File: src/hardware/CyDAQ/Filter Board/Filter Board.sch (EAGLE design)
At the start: 218 parts, among them J1 DCJ0202, J10 Vout_HEADER, J11 5V0_SENSOR, J12 3V3_SENSOR, J13 1V8_SENSOR, J14 BRKOUT_JD, J15 BRKOUT_JC, J16 BRKOUT_JB, J17 BRKOUT_JF, J18 5V0_CONN, J19 3V3_CONN, J2 ZYBO_JF, J20 1V8_CONN, J3 ZYBO_JE, J4 ZYBO_JD, J5 ZYBO_JC, J6 ZYBO_JB, J7 A_XADC, J8 SJ1-3523N, J9 Vin_HEADER, U1 TPS54531DDARDDA8_3P1X2P4-L, U10 CD74HCT4051, U11 CD74HCT4051, U12 OPA4197, U13 OPA4197, U14 OPA4197, U15 OPA4197, U16 OPA4197, U17 CD74HCT4053, U18 CD74HCT4051, U19 OPA2197, U2 VS-50WQ04FNPBFDPAK-L, U3 TPS56339, U4 TPS56339, U5 LM43601PWPR, U6 X9258_A, U7 X925_B, U8 X9258_C, U9 X9258_D

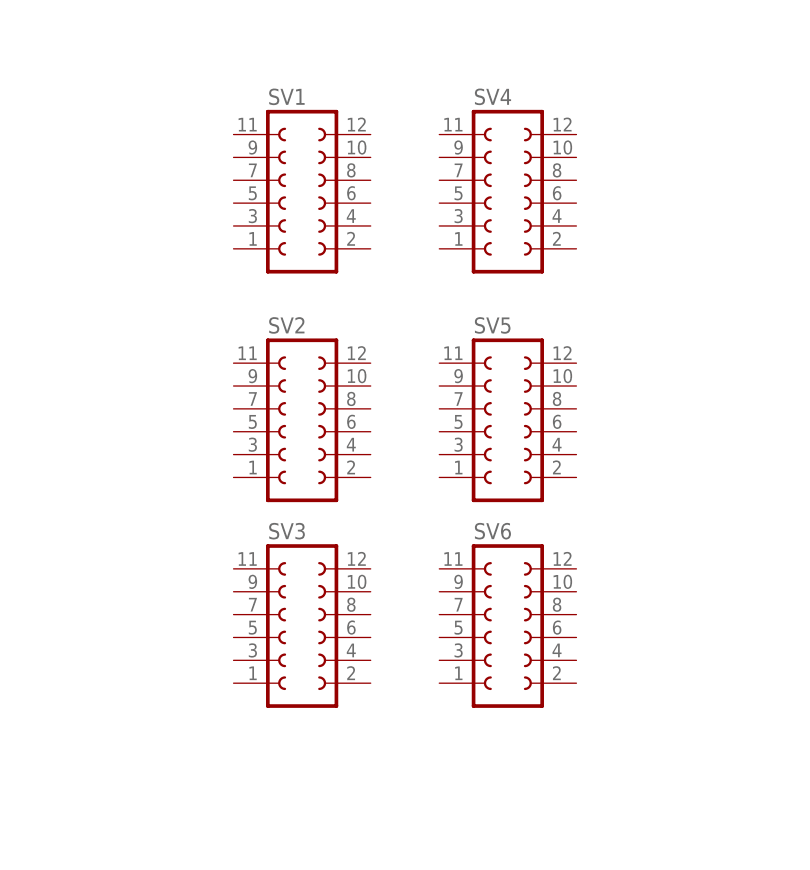
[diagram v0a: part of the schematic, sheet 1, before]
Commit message: Placed components and started routing
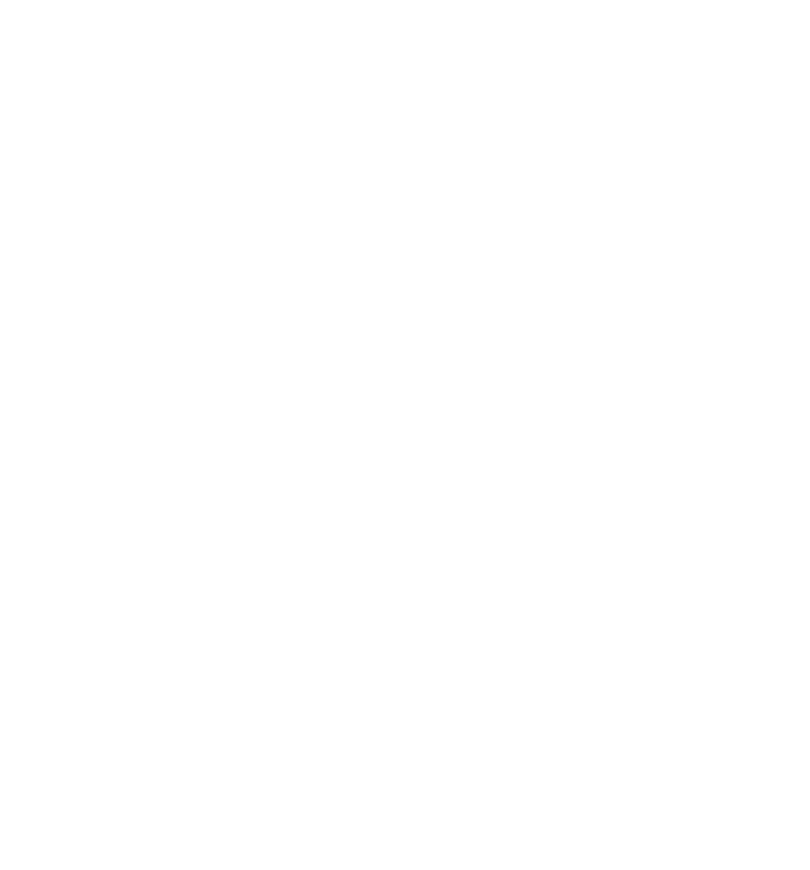
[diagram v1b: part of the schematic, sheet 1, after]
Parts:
- removed SV1, SV2, SV3, SV4, SV5, SV6: (no value), con-lsta:FE06-2
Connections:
- removed net N$60: C44.2, J7.3, J7.4, R61.2, U12_C.OUT, U9_VR1.H, U9_VR1.W
- net 1V8SENSOR_IN: now also U18.A0; no longer U18.A2
- net 3V3SENSOR_IN: now also U18.A1; no longer U18.A0
- net 5V0SENSOR_IN: now also U18.A2; no longer U18.A1
- net GND: now also C44.2, J7.3, J7.4, R61.2, U12_C.OUT, U9_VR1.H, U9_VR1.W
- net SCL: now also R14.1; no longer R15.1
- net SDA: now also R15.1; no longer R14.1
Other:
- note added: "I2C Pullups"
- moved on the sheet: R16, R29

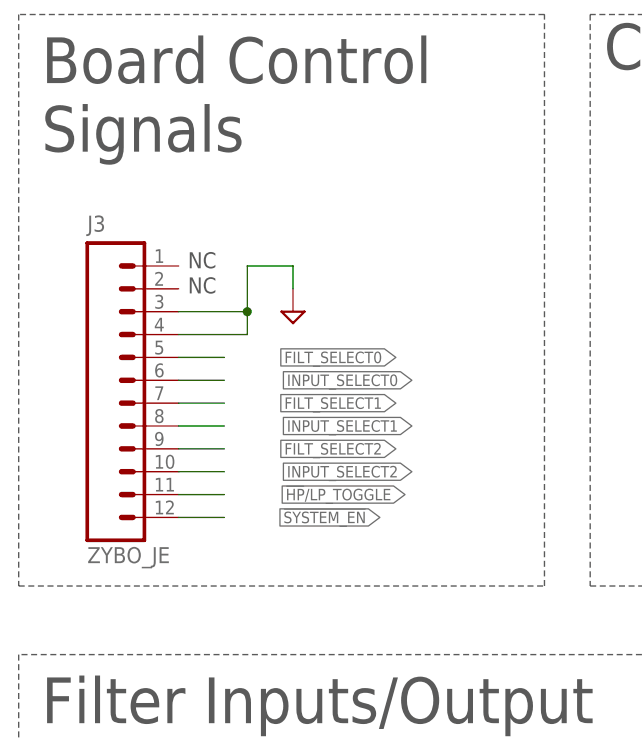
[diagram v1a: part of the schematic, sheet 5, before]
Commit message: Finished routing BP filter
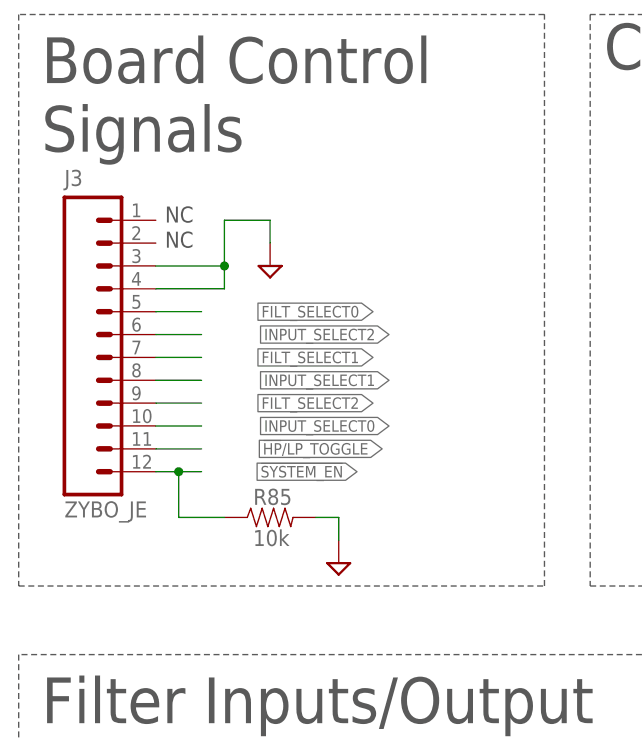
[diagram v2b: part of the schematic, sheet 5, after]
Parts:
- added R85: 10k, Resistors:SMD_0805
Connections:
- new net BP6_HPOUT: C44.2, R61.2, U12_B.OUT, U9_VR1.H, U9_VR1.W
- net !SYSTEM_EN: now also R85.1
- net BP6_OUT: now also U13_D.-IN, U13_D.OUT; no longer U14_A.-IN, U14_A.OUT
- net GND: now also R85.2, U12_B.+IN, U13_C.+IN, U14_B.+IN; no longer C44.2, R61.2, U12_C.OUT, U12_D.+IN, U13_D.+IN, U14_D.+IN, U9_VR1.H, U9_VR1.W
- net HP2_OUT1: now also U14_A.OUT; no longer U14_B.OUT
- net INPUT_SELECT0: now also J3.10; no longer J3.6
- net INPUT_SELECT2: now also J3.6; no longer J3.10
- net LP2_OUT1: now also U14_C.OUT; no longer U14_D.OUT
- net N$22: now also U14_D.+IN; no longer U12_A.+IN
- net N$23: now also U14_D.-IN, U14_D.OUT; no longer U12_A.-IN, U12_A.OUT
- net N$24: now also U12_A.-IN; no longer U12_B.-IN
- net N$25: now also U14_A.+IN; no longer U14_B.+IN
- net N$26: now also U14_A.-IN; no longer U14_B.-IN
- net N$28: now also U14_B.-IN; no longer U14_C.-IN
- net N$29: now also U14_B.OUT; no longer U14_C.OUT
- net N$30: now also U14_C.-IN; no longer U14_D.-IN
- net N$57: now also U12_A.+IN; no longer U12_B.+IN
- net N$58: now also U12_A.OUT, U9_VR2.H, U9_VR2.W; no longer U12_B.OUT, U9_VR0.H, U9_VR0.W
- net N$59: now also U12_B.-IN, U9_VR2.L; no longer U12_C.-IN, U9_VR0.L
- net N$61: now also U12_C.-IN; no longer U12_D.-IN
- net N$62: now also U12_C.OUT, U9_VR0.H, U9_VR0.W; no longer U12_D.OUT, U9_VR2.H, U9_VR2.W
- net N$63: now also U12_D.+IN, U9_VR0.L; no longer U13_A.+IN, U9_VR2.L
- net N$64: now also U12_D.-IN, U12_D.OUT; no longer U13_A.-IN, U13_A.OUT
- net N$65: now also U13_A.-IN; no longer U13_C.-IN
- net N$66: now also U13_A.+IN; no longer U13_C.+IN
- net N$67: now also U13_A.OUT; no longer U13_C.OUT
- net N$68: now also U13_C.-IN; no longer U13_B.-IN
- net N$69: now also U13_C.OUT; no longer U13_B.OUT
- net N$70: now also U13_B.-IN; no longer U13_D.-IN
- net N$71: now also U13_B.OUT; no longer U13_D.OUT
- net N$72: now also U13_D.+IN; no longer U14_A.+IN
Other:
- moved on the sheet: J3, U12_B, U12_C, U12_D, U13_A, U13_B, U13_C, U13_D, U14_B, U14_C, U14_D, U9_VR0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

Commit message: Continued routing ~ 80% done
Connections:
- net FILTER_IN: now also U16_B.+IN; no longer U16_C.+IN
- net FILTER_OUT_BUFF: now also U16_C.-IN, U16_C.OUT; no longer U16_D.-IN, U16_D.OUT
- net GND: now also U15_D.+IN, U16_D.+IN, U6_VR1.L, U7_VR3.L; no longer U15_B.+IN, U16_B.+IN, U6_VR2.L, U7_VR1.L
- net HP2_OUT2: now also U15_B.OUT, U8_VR3.H, U8_VR3.W; no longer U15_A.OUT, U8_VR2.H, U8_VR2.W
- net HP2_OUT3: now also U15_A.OUT; no longer U15_D.OUT
- net LP1_IN: now also U6_VR2.H, U6_VR2.W; no longer U6_VR1.H, U6_VR1.W
- net LP1_OUT: now also U6_VR2.L; no longer U6_VR1.L
- net LP2_OUT1: now also U14_B.OUT; no longer U14_C.OUT
- net LP2_OUT2: now also U15_D.OUT; no longer U15_C.OUT
- net LP2_OUT3: now also U16_D.OUT; no longer U16_B.OUT
- net N$22: now also U6_VR1.H, U6_VR1.W; no longer U6_VR2.H, U6_VR2.W
- net N$28: now also U14_C.-IN; no longer U14_B.-IN
- net N$29: now also U14_C.OUT, U7_VR1.H, U7_VR1.W; no longer U14_B.OUT, U7_VR3.H, U7_VR3.W
- net N$30: now also U14_B.-IN, U7_VR1.L; no longer U14_C.-IN, U7_VR3.L
- net N$31: now also U15_B.+IN; no longer U15_A.+IN
- net N$32: now also U15_B.-IN; no longer U15_A.-IN
- net N$34: now also U15_C.-IN, U8_VR3.L; no longer U15_B.-IN, U8_VR2.L
- net N$35: now also U15_C.OUT, U8_VR2.H, U8_VR2.W; no longer U15_B.OUT, U8_VR3.H, U8_VR3.W
- net N$36: now also U15_D.-IN, U8_VR2.L; no longer U15_C.-IN, U8_VR3.L
- net N$37: now also U15_A.+IN; no longer U15_D.+IN
- net N$38: now also U15_A.-IN; no longer U15_D.-IN
- net N$42: now also U16_D.-IN; no longer U16_B.-IN
- net N$43: now also U16_C.+IN; no longer U16_D.+IN
- net N$72: now also U7_VR3.H, U7_VR3.W; no longer U7_VR1.H, U7_VR1.W
- net VIN_BUFFERED: now also U16_B.-IN, U16_B.OUT; no longer U16_C.-IN, U16_C.OUT
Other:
- note removed: "TODO: Add voltage protection"
- moved on the sheet: U14_B, U14_C, U15_A, U15_B, U15_C, U15_D, U16_C, U6_VR1, U6_VR2, U8_VR2, U8_VR3

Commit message: Used Gateswap magic to clean up some routing
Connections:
- net HP2_OUT1: now also U7_VR1.H, U7_VR1.W; no longer U7_VR2.H, U7_VR2.W
- net LP2_OUT1: now also U14_C.OUT; no longer U14_B.OUT
- net N$28: now also U14_B.-IN, U7_VR1.L; no longer U14_C.-IN, U7_VR2.L
- net N$29: now also U14_B.OUT, U7_VR2.H, U7_VR2.W; no longer U14_C.OUT, U7_VR1.H, U7_VR1.W
- net N$30: now also U14_C.-IN, U7_VR2.L; no longer U14_B.-IN, U7_VR1.L
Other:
- moved on the sheet: U14_B, U14_C, U7_VR1, U7_VR2
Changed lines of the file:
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@@
 </instance>
 <instance part="SUPPLY58" gate="GND" x="172.72" y="22.86" smashed="yes"/>
-<instance part="U7" gate="_VR2" x="116.84" y="220.98" smashed="yes" rot="R90">
+<instance part="U7" gate="_VR1" x="116.84" y="220.98" smashed="yes" rot="R90">
 <attribute name="NAME" x="106.934" y="225.552" size="1.778" layer="95"/>
 <attribute name="VALUE" x="113.03" y="215.646" size="1.778" layer="95"/>
@@
 <attribute name="NAME" x="92.71" y="207.518" size="1.778" layer="95"/>
 </instance>
-<instance part="U14" gate="_C" x="137.16" y="205.74" smashed="yes">
+<instance part="U14" gate="_B" x="137.16" y="205.74" smashed="yes">
 <attribute name="VALUE" x="140.97" y="202.438" size="1.778" layer="96"/>
 <attribute name="NAME" x="140.97" y="207.518" size="1.778" layer="95"/>
 </instance>
-<instance part="U14" gate="_B" x="187.96" y="205.74" smashed="yes">
+<instance part="U14" gate="_C" x="187.96" y="205.74" smashed="yes">
 <attribute name="VALUE" x="191.77" y="202.438" size="1.778" layer="96"/>
 <attribute name="NAME" x="191.77" y="207.518" size="1.778" layer="95"/>
@@
 <attribute name="NAME" x="191.77" y="103.378" size="1.778" layer="95"/>
 </instance>
-<instance part="U7" gate="_VR1" x="167.64" y="220.98" smashed="yes" rot="R90">
+<instance part="U7" gate="_VR2" x="167.64" y="220.98" smashed="yes" rot="R90">
 <attribute name="NAME" x="157.988" y="225.298" size="1.778" layer="95"/>
 <attribute name="VALUE" x="164.084" y="215.9" size="1.778" layer="95"/>
@@
 <wire x1="127" y1="200.66" x2="127" y2="203.2" width="0.1524" layer="91"/>
 <wire x1="127" y1="203.2" x2="129.54" y2="203.2" width="0.1524" layer="91"/>
-<pinref part="U14" gate="_C" pin="+IN"/>
+<pinref part="U14" gate="_B" pin="+IN"/>
 </segment>
 <segment>
@@
 <wire x1="177.8" y1="200.66" x2="177.8" y2="203.2" width="0.1524" layer="91"/>
 <wire x1="177.8" y1="203.2" x2="180.34" y2="203.2" width="0.1524" layer="91"/>
-<pinref part="U14" gate="_B" pin="+IN"/>
+<pinref part="U14" gate="_C" pin="+IN"/>
 </segment>
 <segment>
@@
 <net name="HP2_OUT1" class="0">
 <segment>
-<pinref part="U7" gate="_VR2" pin="W"/>
+<pinref part="U7" gate="_VR1" pin="W"/>
 <wire x1="116.84" y1="226.06" x2="116.84" y2="228.6" width="0.1524" layer="91"/>
 <wire x1="116.84" y1="228.6" x2="104.14" y2="228.6" width="0.1524" layer="91"/>
 <wire x1="104.14" y1="228.6" x2="104.14" y2="220.98" width="0.1524" layer="91"/>
-<pinref part="U7" gate="_VR2" pin="H"/>
+<pinref part="U7" gate="_VR1" pin="H"/>
 <wire x1="104.14" y1="220.98" x2="111.76" y2="220.98" width="0.1524" layer="91"/>
 <pinref part="R42" gate="G$1" pin="2"/>
@@
 <net name="N$28" class="0">
 <segment>
-<pinref part="U7" gate="_VR2" pin="L"/>
+<pinref part="U7" gate="_VR1" pin="L"/>
 <wire x1="121.92" y1="220.98" x2="127" y2="220.98" width="0.1524" layer="91"/>
-<pinref part="U14" gate="_C" pin="-IN"/>
+<pinref part="U14" gate="_B" pin="-IN"/>
 <wire x1="127" y1="220.98" x2="127" y2="208.28" width="0.1524" layer="91"/>
 <wire x1="127" y1="208.28" x2="129.54" y2="208.28" width="0.1524" layer="91"/>
@@
 <net name="N$29" class="0">
 <segment>
-<pinref part="U14" gate="_C" pin="OUT"/>
+<pinref part="U14" gate="_B" pin="OUT"/>
 <wire x1="144.78" y1="205.74" x2="152.4" y2="205.74" width="0.1524" layer="91"/>
 <pinref part="R45" gate="G$1" pin="2"/>
@@
 <wire x1="154.94" y1="228.6" x2="154.94" y2="220.98" width="0.1524" layer="91"/>
 <junction x="154.94" y="220.98"/>
-<pinref part="U7" gate="_VR1" pin="H"/>
-<pinref part="U7" gate="_VR1" pin="W"/>
+<pinref part="U7" gate="_VR2" pin="H"/>
+<pinref part="U7" gate="_VR2" pin="W"/>
 </segment>
 </net>
@@
 <pinref part="C33" gate="G$1" pin="1"/>
 <wire x1="172.72" y1="220.98" x2="177.8" y2="220.98" width="0.1524" layer="91"/>
-<pinref part="U14" gate="_B" pin="-IN"/>
+<pinref part="U14" gate="_C" pin="-IN"/>
 <wire x1="177.8" y1="220.98" x2="185.42" y2="220.98" width="0.1524" layer="91"/>
 <wire x1="180.34" y1="208.28" x2="177.8" y2="208.28" width="0.1524" layer="91"/>
 <wire x1="177.8" y1="208.28" x2="177.8" y2="220.98" width="0.1524" layer="91"/>
 <junction x="177.8" y="220.98"/>
-<pinref part="U7" gate="_VR1" pin="L"/>
+<pinref part="U7" gate="_VR2" pin="L"/>
 </segment>
 </net>
@@
 <pinref part="C33" gate="G$1" pin="2"/>
 <wire x1="193.04" y1="220.98" x2="200.66" y2="220.98" width="0.1524" layer="91"/>
-<pinref part="U14" gate="_B" pin="OUT"/>
+<pinref part="U14" gate="_C" pin="OUT"/>
 <wire x1="200.66" y1="220.98" x2="200.66" y2="205.74" width="0.1524" layer="91"/>
 <wire x1="200.66" y1="205.74" x2="195.58" y2="205.74" width="0.1524" layer="91"/>
